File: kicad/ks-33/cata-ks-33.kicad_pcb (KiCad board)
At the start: 2 copper layers, 209 x 76 mm, 81 parts, among them SW1 SW_Push, SW10 SW_Push, SW11 SW_Push, SW12 SW_Push, SW13 SW_Push, SW14 SW_Push, SW15 SW_Push, SW16 SW_Push, SW17 SW_Push, SW18 SW_Push, SW19 SW_Push, SW2 SW_Push, SW20 SW_Push, SW21 SW_Push, SW22 SW_Push, SW23 SW_Push, SW24 SW_Push, SW25 SW_Push, SW26 SW_Push, SW27 SW_Push, SW28 SW_Push, SW29 SW_Push, SW3 SW_Push, SW30 SW_Push, SW31 SW_Push, SW32 SW_Push, SW33 SW_Push, SW34 SW_Push, SW4 SW_Push, SW5 SW_Push, SW6 SW_Push, SW7 SW_Push, SW8 SW_Push, SW9 SW_Push, U1 RP2040-Zero

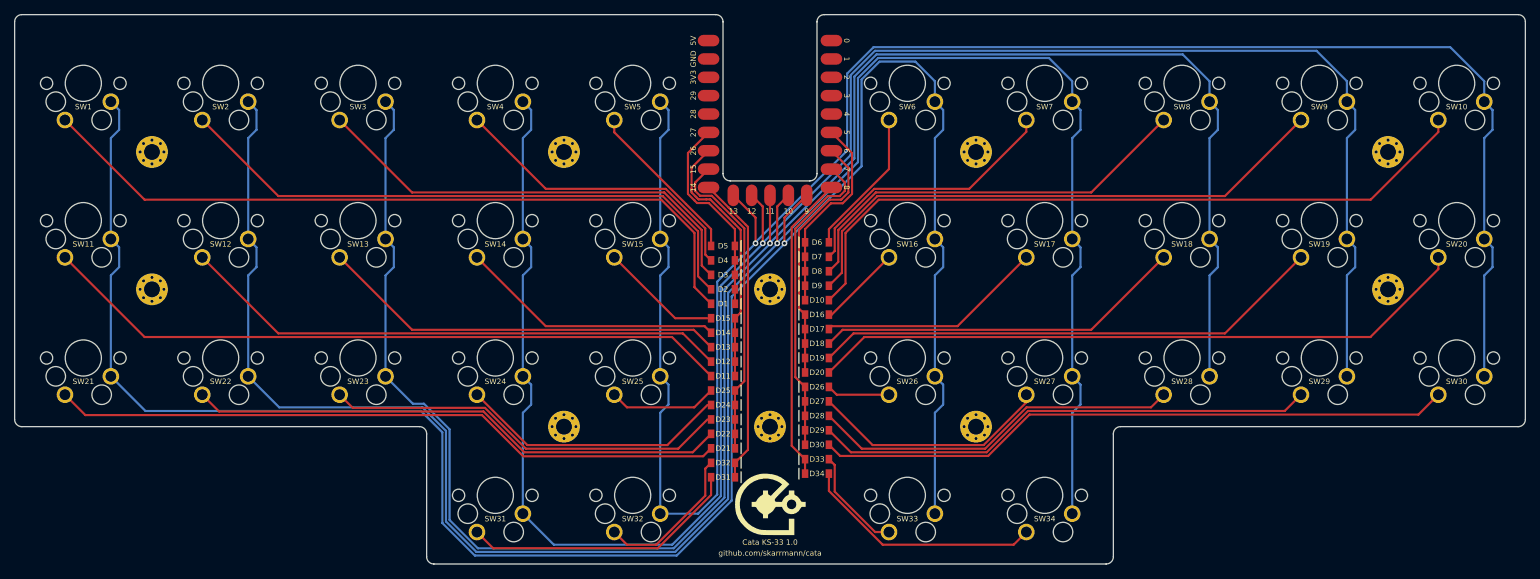
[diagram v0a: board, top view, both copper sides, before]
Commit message: Fix diode alignment, generate gerbers
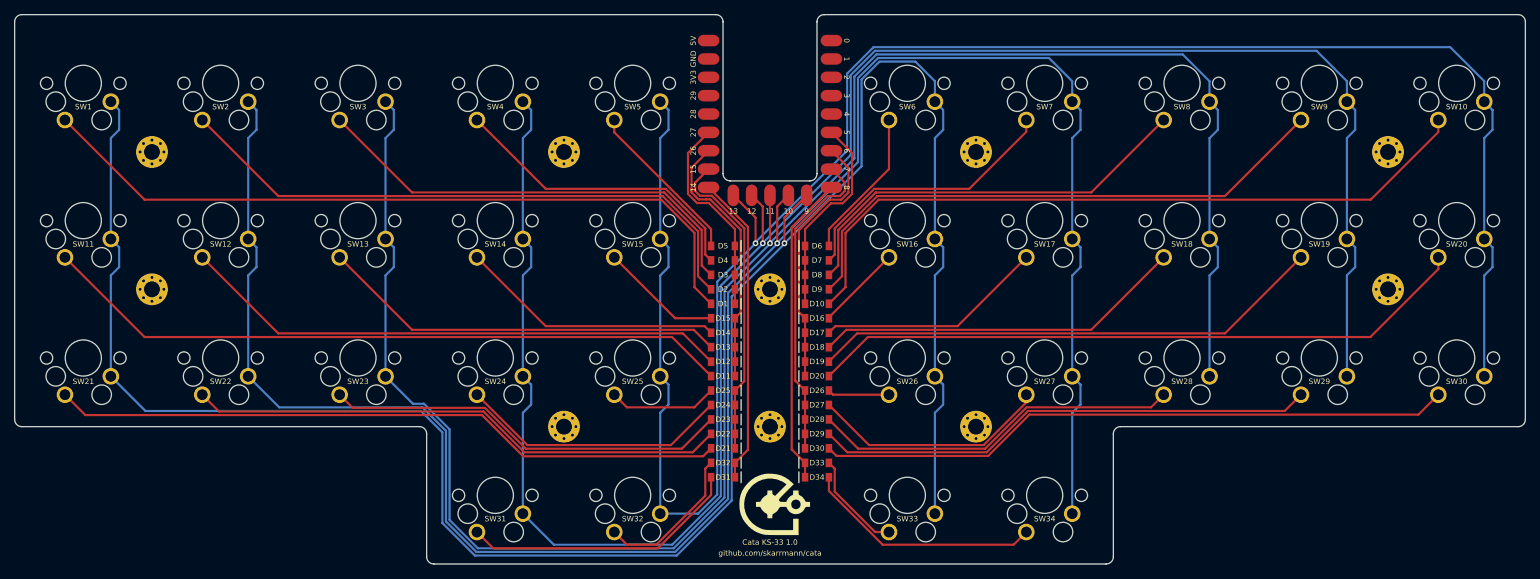
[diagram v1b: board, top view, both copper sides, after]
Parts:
- moved LOGO1 0.60 mm to (149.1, 135.0)
- moved D10 0.50 mm to (155.0, 107.2)
- moved D16 0.50 mm to (155.0, 109.2)
- moved D17 0.50 mm to (155.0, 111.2)
- moved D18 0.50 mm to (155.0, 113.2)
- moved D19 0.50 mm to (155.0, 115.2)
- moved D20 0.50 mm to (155.0, 117.2)
- moved D26 0.50 mm to (155.0, 119.2)
- moved D27 0.50 mm to (155.0, 121.2)
- moved D28 0.50 mm to (155.0, 123.2)
- moved D29 0.50 mm to (155.0, 125.2)
- moved D30 0.50 mm to (155.0, 127.2)
- moved D33 0.50 mm to (155.0, 129.2)
- moved D34 0.50 mm to (155.0, 131.2)
- moved D6 0.50 mm to (155.0, 99.2)
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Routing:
- net ROW8: track 42.6 -> 43.1 mm
- net ROW6: track 43.2 -> 43.7 mm
- net ROW4: track 35.8 -> 36.3 mm
- net ROW2: track 28.0 -> 28.5 mm
- net Net-(D8-A): track 57.6 -> 58.1 mm
- net Net-(D7-A): track 37.9 -> 38.4 mm
- net Net-(D6-A): track 20.4 -> 20.9 mm
- net Net-(D34-A): track 33.5 -> 33.0 mm
- net Net-(D33-A): track 14.6 -> 14.1 mm
- net Net-(D24-A): track 37.1 -> 37.6 mm
- net Net-(D23-A): track 55.7 -> 56.2 mm
- net Net-(D15-A): track 16.4 -> 16.9 mm
- net Net-(D10-A): track 99.7 -> 100.2 mm

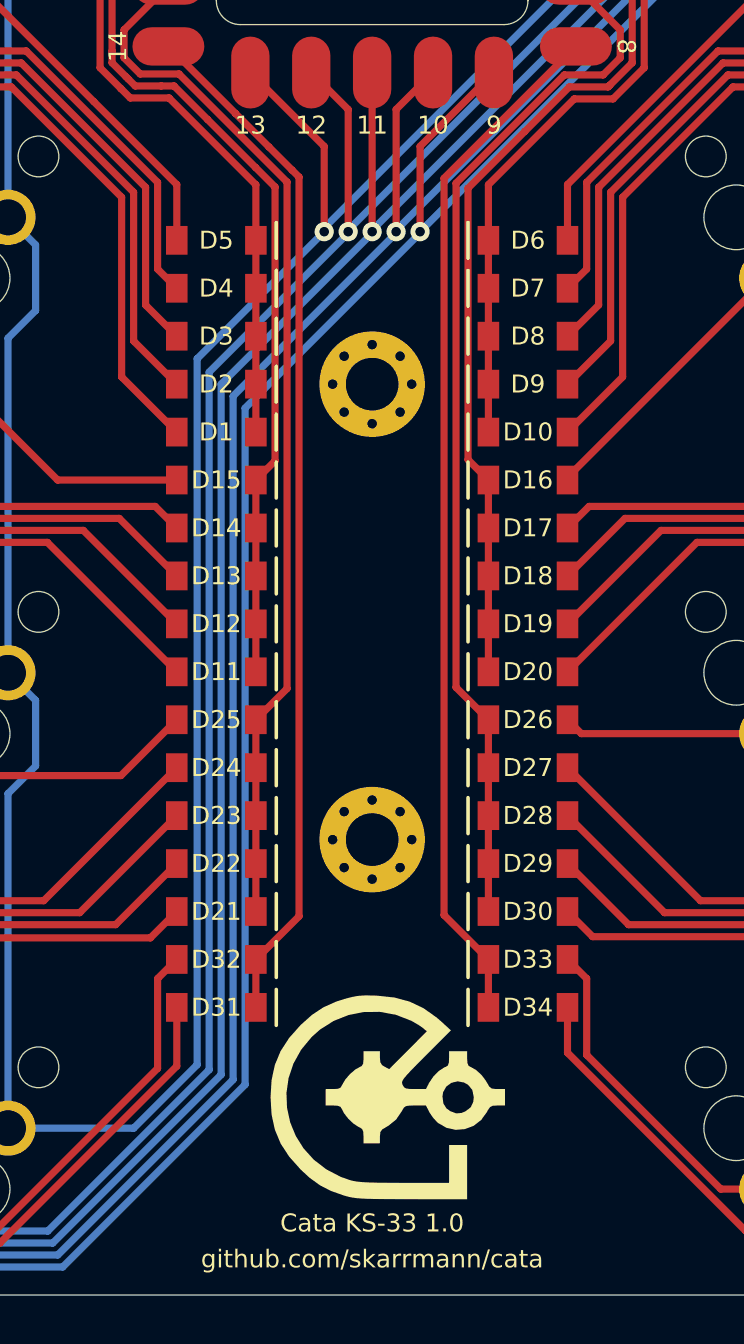
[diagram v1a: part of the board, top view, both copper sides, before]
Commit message: Move logo and name silkscreen on PCB
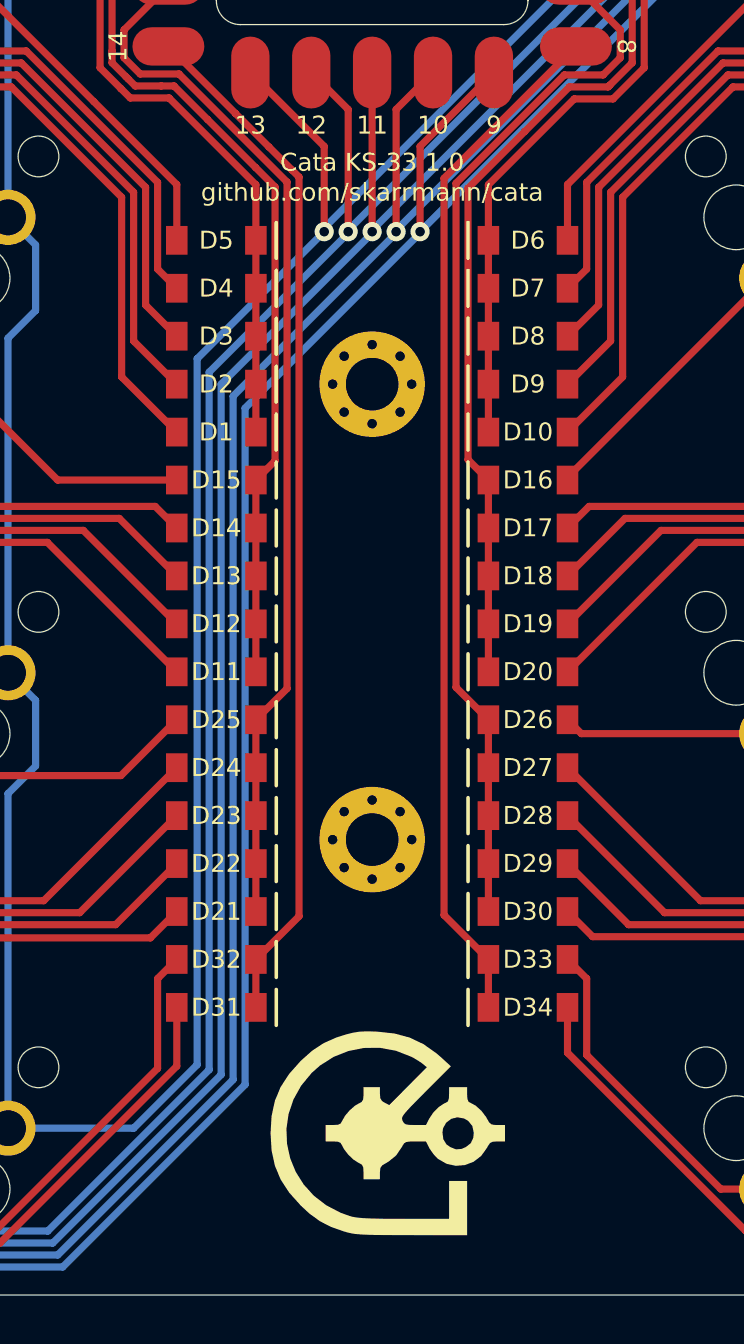
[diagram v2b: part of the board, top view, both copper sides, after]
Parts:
- moved LOGO1 1.50 mm to (149.1, 136.5)
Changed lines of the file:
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@@
 	(footprint "cata-footprints:Logo_Cata"
 		(layer "F.Cu")
-		(at 149.1 135)
+		(at 149.1 136.5)
 		(property "Reference" "LOGO1"
 			(at 0 2 0)
@@
 	)
 	(gr_text "Cata KS-33 1.0"
-		(at 148.5 140.25 0)
+		(at 148.5 96 0)
 		(layer "F.SilkS")
 		(effects
@@
 	)
 	(gr_text "github.com/skarrmann/cata\n"
-		(at 148.5 141.75 0)
+		(at 148.5 97.25 0)
 		(layer "F.SilkS")
 		(effects
